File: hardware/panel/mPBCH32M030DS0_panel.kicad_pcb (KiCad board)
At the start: 2 copper layers, 97.9 x 95.6 mm, 315 parts, among them J1 EDGE_L, J1 SOCK_L, J2 EDGE_R, J2 SOCK_R, J3 PWR_IN, J4 MOTOR, J8 USB-C, Q1 MTN2306AN3, Q1 TKR74F04PB, Q1 TPN1R603PL, Q10 TPN1R603PL, Q2 MTN2306AN3, Q2 TKR74F04PB, Q2 TPN1R603PL, Q3 MTN2306AN3, Q3 TKR74F04PB, Q3 TPN1R603PL, Q4 MTN2306AN3, Q4 TKR74F04PB, Q4 TPN1R603PL, Q5 MTN2306AN3, Q5 TKR74F04PB, Q5 TPN1R603PL, Q6 MTN2306AN3, Q6 TKR74F04PB, Q6 TPN1R603PL, Q7 MTN2306AN3, Q7 TKR74F04PB, Q7 TPN1R603PL, Q8 MTN2306AN3, Q8 TKR74F04PB, Q8 TPN1R603PL, Q9 TPN2R304PL, SW1 RESET, SW2 USER/BOOT, U1 CH32M030C8U7, U2 78L05, U3 USBLC6-2SC6, U4 LM74700-Q1, U5 LM74700-Q1, Y1 8MHz CL=20pF

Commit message: 面付けパネルを A/C 74.9mm に合わせて更新, 製造データと資料を最新の A/C に
- gen_panel.py: A/C の長さ 70.74 → 74.9mm (パネル 97.9 × 99.8mm)。タブを銅の無い区間へ移動
  (A の右辺は J2 沿いの GND 配線があるため A↔C / C↔B のタブは下寄り)
- 各基板の製造データ (hardware/fab/*.zip) と DRC 集計を再生成
- README / stacking.md: A/C の寸法・電流の目安 (A 約 5A/相 はんだ盛り時, C 約 3A/相) とレイアウトの説明,
  電源ベタのはんだ盛りの注意 (低温はんだ不可, 下面は盛り 0.3〜0.5mm 以下), J3/J4 の向き, D9 を外した理由
- B はレイアウト見直し中と明記 (現状の配線は約 1A まで)

Co-Authored-By: Claude Opus 5.5 <noreply@anthropic.com>
Claude-Session: https://claude.ai/code/session_01LENFjjhDfYjJZV1NWhB9uV
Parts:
- removed the C1 at (39.9, 45.7)
- removed the C1 at (15.1, 55.3)
- removed the C3 at (15.4, 10.4)
- removed the C3 at (40.3, 10.4)
- removed the C30 at (17.8, 46.1)
- removed the C30 at (42.7, 45.7)
- removed the C31 at (18.6, 42.5)
- removed the C31 at (40.4, 42.1)
- removed the C4 at (18.1, 10.1)
- removed the C4 at (43.0, 10.1)
- removed the C40 at (17.8, 34.4)
- removed the C40 at (42.7, 34.1)
- removed the C41 at (40.4, 30.5)
- removed the C41 at (18.6, 30.8)
- removed the C5 at (18.8, 41.0)
- removed the C5 at (43.7, 31.4)
- removed the C50 at (42.7, 22.5)
- removed the C50 at (17.8, 22.7)
- removed the C51 at (40.4, 18.9)
- removed the C51 at (18.6, 19.1)
- removed the C6 at (17.7, 5.79)
- removed the C6 at (42.6, 5.79)
- removed the C60 at (42.7, 10.8)
- removed the C60 at (17.8, 11.0)
- removed the C61 at (18.6, 7.39)
- removed the C61 at (40.4, 7.24)
- removed the C7 at (14.8, 24.0)
- removed the C7 at (39.7, 24.0)
- removed the C71 at (37.2, 22.5)
- removed the C71 at (15.2, 53.8)
- removed the C72 at (38.4, 34.1)
- removed the C72 at (18.7, 53.8)
- removed the C73 at (37.2, 45.7)
- removed the C73 at (22.2, 53.8)
- removed the C8 at (14.8, 33.6)
- removed the D1 at (11.7, 48.6)
- removed the D1 at (36.6, 39.0)
- removed the D9 at (37.9, 7.08)
- removed the D9 at (13.0, 7.08)
- removed the F1 at (38.4, 32.7)
- removed the F1 at (13.5, 42.3)
- removed the F3 at (37.3, 2.60)
- removed the F3 at (12.4, 2.60)
- removed the J3 at (34.9, 62.1)
- removed the J3 at (10.1, 62.1)
- removed the J4 at (32.4, 68.7)
- removed the J4 at (7.55, 68.7)
- removed the JP5 at (40.5, 50.1)
- removed the JP5 at (18.7, 50.3)
- removed the JP7 at (35.6, 55.0)
- removed the JP7 at (10.7, 55.2)
- removed the MB at (0.00, 0.00) (x9)
- removed the Q1 at (11.7, 38.1)
- removed the Q1 at (36.3, 37.8)
- removed the Q10 at (17.9, 2.42)
- removed the Q10 at (42.8, 2.42)
- removed the Q2 at (16.5, 38.1)
- removed the Q2 at (40.6, 37.8)
- removed the Q3 at (11.7, 26.4)
- removed the Q3 at (36.3, 26.2)
- removed the Q4 at (16.5, 26.4)
- removed the Q4 at (40.6, 26.2)
- removed the Q5 at (11.7, 14.7)
- removed the Q5 at (36.3, 14.6)
- removed the Q6 at (40.6, 14.6)
- removed the Q6 at (16.5, 14.7)
- removed the Q7 at (36.3, 2.94)
- removed the Q7 at (11.7, 3.02)
- removed the Q8 at (40.6, 2.94)
- removed the Q8 at (16.5, 3.02)
- removed the Q9 at (41.4, 37.1)
- removed the Q9 at (16.5, 46.7)
- removed the R11 at (10.4, 39.3)
- removed the R11 at (35.3, 29.7)
- removed the R12 at (12.6, 39.3)
- removed the R12 at (37.5, 29.7)
- removed the R30 at (22.9, 46.1)
- removed the R30 at (47.8, 45.7)
- removed the R31 at (19.1, 46.1)
- removed the R31 at (43.9, 45.7)
- removed the R32 at (46.5, 45.7)
- removed the R32 at (21.6, 46.1)
- removed the R33 at (20.4, 46.1)
- removed the R33 at (45.2, 45.7)
- removed the R34 at (36.6, 40.9)
- removed the R34 at (13.3, 42.1)
- removed the R40 at (22.9, 34.4)
- removed the R40 at (47.8, 34.1)
- removed the R41 at (43.9, 34.1)
- removed the R41 at (19.1, 34.4)
- removed the R42 at (21.6, 34.4)
- removed the R42 at (46.5, 34.1)
- removed the R43 at (45.2, 34.1)
- removed the R43 at (20.4, 34.4)
- removed the R44 at (36.6, 29.3)
- removed the R44 at (13.3, 30.4)
- removed the R50 at (22.9, 22.7)
- removed the R50 at (47.8, 22.5)
- removed the R51 at (43.9, 22.5)
- removed the R51 at (19.1, 22.7)
- removed the R52 at (46.5, 22.5)
- removed the R52 at (21.6, 22.7)
- removed the R53 at (45.2, 22.5)
- removed the R53 at (20.4, 22.7)
- removed the R54 at (13.3, 18.7)
- removed the R54 at (36.6, 17.7)
- removed the R6 at (19.9, 5.80)
- removed the R6 at (44.8, 5.80)
- removed the R60 at (22.9, 11.0)
- removed the R60 at (47.8, 10.9)
- removed the R61 at (19.1, 11.0)
- removed the R61 at (43.9, 10.9)
- removed the R62 at (46.5, 10.9)
- removed the R62 at (21.6, 11.0)
- removed the R63 at (45.2, 10.9)
- removed the R63 at (20.4, 11.0)
- removed the R64 at (13.3, 7.01)
- removed the R64 at (36.6, 6.05)
- removed the R70 at (36.6, 48.9)
- removed the R70 at (13.3, 49.9)
- removed the R71 at (12.8, 53.8)
- removed the R71 at (34.8, 22.5)
- removed the R72 at (14.0, 53.8)
- removed the R72 at (36.0, 22.5)
- removed the R74 at (36.0, 34.1)
- removed the R74 at (16.3, 53.8)
- removed the R75 at (17.5, 53.8)
- removed the R75 at (37.2, 34.1)
- removed the R77 at (34.8, 45.7)
- removed the R77 at (19.8, 53.8)
- removed the R78 at (36.0, 45.7)
- removed the R78 at (21.0, 53.8)
- removed the TH1 at (34.8, 34.1)
- removed the TH1 at (9.96, 34.4)
- removed the U2 at (37.2, 16.3)
- removed the U2 at (12.3, 16.3)
- removed the U4 at (11.5, 54.7)
- removed the U4 at (36.4, 45.1)
- removed the U5 at (36.4, 11.3)
- removed the U5 at (11.5, 11.3)
- added C1: 10uF/50V, C_1206_3216Metric, B.Cu at (38.5, 70.4)
- added C1: 10uF/50V, C_1206_3216Metric, B.Cu at (13.6, 70.4)
- added C120: 1nF/50V, C_0402_1005Metric, B.Cu at (31.4, 87.0)
- added C3: 1uF/50V, C_0603_1608Metric, B.Cu at (22.1, 2.12)
- added C3: 1uF/50V, C_0603_1608Metric, B.Cu at (46.9, 2.12)
- added C30: 0.1uF/50V, C_0402_1005Metric, B.Cu at (11.4, 42.4)
- added C30: 0.1uF/50V, C_0402_1005Metric, B.Cu at (36.5, 42.4)
- added C31: 10uF/25V, C_0805_2012Metric, B.Cu at (12.9, 42.4)
- added C31: 10uF/25V, C_0805_2012Metric, B.Cu at (38.2, 42.0)
- added C4: 1uF/25V, C_0402_1005Metric, B.Cu at (21.8, 4.75)
- added C4: 1uF/25V, C_0402_1005Metric, B.Cu at (46.7, 4.75)
- added C40: 0.1uF/50V, C_0402_1005Metric, B.Cu at (36.5, 33.4)
- added C40: 0.1uF/50V, C_0402_1005Metric, B.Cu at (11.4, 33.4)
- added C41: 10uF/25V, C_0805_2012Metric, B.Cu at (38.2, 33.0)
- added C41: 10uF/25V, C_0805_2012Metric, B.Cu at (12.9, 33.4)
- added C5: 0.1uF/50V, C_0402_1005Metric, B.Cu at (12.9, 60.8)
- added C5: 0.1uF/50V, C_0402_1005Metric, B.Cu at (37.8, 60.8)
- added C50: 0.1uF/50V, C_0402_1005Metric, B.Cu at (11.4, 24.4)
- added C50: 0.1uF/50V, C_0402_1005Metric, B.Cu at (36.5, 24.4)
- added C51: 10uF/25V, C_0805_2012Metric, B.Cu at (38.2, 24.0)
- added C51: 10uF/25V, C_0805_2012Metric, B.Cu at (12.9, 24.4)
- added C6: 0.1uF/50V, C_0402_1005Metric, B.Cu at (13.2, 8.95)
- added C6: 0.1uF/50V, C_0402_1005Metric, B.Cu at (38.1, 8.95)
- added C60: 0.1uF/50V, C_0402_1005Metric, B.Cu at (36.5, 15.4)
- added C60: 0.1uF/50V, C_0402_1005Metric, B.Cu at (11.4, 15.4)
- added C61: 10uF/25V, C_0805_2012Metric, B.Cu at (12.9, 15.4)
- added C61: 10uF/25V, C_0805_2012Metric, B.Cu at (38.2, 15.0)
- added C7: 100uF/25V, CP_Elec_8x6.2, F.Cu at (39.8, 4.72)
- added C7: 150uF/25V, CP_Elec_8x6.2, F.Cu at (14.9, 4.72)
- added C71: 1nF/50V, C_0402_1005Metric, B.Cu at (12.9, 48.1)
- added C71: 1nF/50V, C_0402_1005Metric, B.Cu at (37.8, 48.1)
- added C72: 1nF/50V, C_0402_1005Metric, B.Cu at (37.8, 50.2)
- added C72: 1nF/50V, C_0402_1005Metric, B.Cu at (12.9, 50.2)
- added C73: 1nF/50V, C_0402_1005Metric, B.Cu at (12.9, 52.4)
- added C73: 1nF/50V, C_0402_1005Metric, B.Cu at (37.8, 52.4)
- added D1: SMBJ16A, D_SMB, B.Cu at (38.5, 65.2)
- added D1: SMBJ16A, D_SMB, B.Cu at (13.6, 65.2)
- added F1: 5A, Fuse_Littelfuse_NANO2_2410, F.Cu at (39.1, 63.1)
- added F1: 7A, Fuse_Littelfuse_NANO2_2410, F.Cu at (14.2, 63.1)
- added F3: 5A, Fuse_1812_4532Metric, B.Cu at (13.4, 2.60)
- added F3: 5A, Fuse_1812_4532Metric, B.Cu at (38.3, 2.60)
- added J3: PWR_IN, PinHeader_2x06_P2.54mm_Vertical, F.Cu at (10.1, 68.4)
- added J3: PWR_IN, PinHeader_2x06_P2.54mm_Vertical, F.Cu at (34.9, 68.4)
- added J4: MOTOR, PinHeader_2x08_P2.54mm_Vertical, F.Cu at (50.2, 73.5)
- added J4: MOTOR, PinHeader_2x08_P2.54mm_Vertical, F.Cu at (25.3, 73.5)
- added JP5: ISEL_B, SolderJumper-3_P1.3mm_Bridged12_RoundedPad1.0x1.5mm_NumberLabels, F.Cu at (11.0, 27.0)
- added JP5: ISEL_B, SolderJumper-3_P1.3mm_Bridged12_RoundedPad1.0x1.5mm_NumberLabels, F.Cu at (35.9, 27.0)
- added JP7: ISEL_A, SolderJumper-3_P1.3mm_Bridged12_RoundedPad1.0x1.5mm_NumberLabels, F.Cu at (11.0, 42.6)
- added JP7: ISEL_A, SolderJumper-3_P1.3mm_Bridged12_RoundedPad1.0x1.5mm_NumberLabels, F.Cu at (35.9, 42.6)
- added MB (x9): , , F.Cu at (0.00, 0.00)
- added Q1: TPN1R603PL, Vishay_PowerPAK_1212-8_Single, B.Cu at (16.3, 44.0)
- added Q1: MTN2306AN3, SOT-23, B.Cu at (41.2, 40.2)
- added Q10: TPN1R603PL, Vishay_PowerPAK_1212-8_Single, B.Cu at (43.7, 2.42)
- added Q10: TPN1R603PL, Vishay_PowerPAK_1212-8_Single, B.Cu at (18.9, 2.42)
- added Q2: MTN2306AN3, SOT-23, B.Cu at (41.2, 43.9)
- added Q2: TPN1R603PL, Vishay_PowerPAK_1212-8_Single, B.Cu at (16.3, 40.2)
- added Q3: TPN1R603PL, Vishay_PowerPAK_1212-8_Single, B.Cu at (16.3, 35.0)
- added Q3: MTN2306AN3, SOT-23, B.Cu at (41.2, 31.2)
- added Q4: MTN2306AN3, SOT-23, B.Cu at (41.2, 34.9)
- added Q4: TPN1R603PL, Vishay_PowerPAK_1212-8_Single, B.Cu at (16.3, 31.2)
- added Q5: TPN1R603PL, Vishay_PowerPAK_1212-8_Single, B.Cu at (16.3, 26.0)
- added Q5: MTN2306AN3, SOT-23, B.Cu at (41.2, 22.2)
- added Q6: MTN2306AN3, SOT-23, B.Cu at (41.2, 25.9)
- added Q6: TPN1R603PL, Vishay_PowerPAK_1212-8_Single, B.Cu at (16.3, 22.2)
- added Q7: TPN1R603PL, Vishay_PowerPAK_1212-8_Single, B.Cu at (16.3, 17.0)
- added Q7: MTN2306AN3, SOT-23, B.Cu at (41.2, 13.2)
- added Q8: MTN2306AN3, SOT-23, B.Cu at (41.2, 16.9)
- added Q8: TPN1R603PL, Vishay_PowerPAK_1212-8_Single, B.Cu at (16.3, 13.2)
- added Q9: TPN2R304PL, Vishay_PowerPAK_1212-8_Single, F.Cu at (14.2, 56.6)
- added Q9: TPN2R304PL, Vishay_PowerPAK_1212-8_Single, F.Cu at (39.1, 56.6)
- added R11: 110k 1%, R_0402_1005Metric, B.Cu at (38.9, 47.9)
- added R11: 110k 1%, R_0402_1005Metric, B.Cu at (14.3, 46.5)
- added R12: 10k 1%, R_0402_1005Metric, B.Cu at (40.2, 47.9)
- added R12: 10k 1%, R_0402_1005Metric, B.Cu at (16.3, 46.5)
- added R30: 47R, R_0402_1005Metric, B.Cu at (44.4, 39.3)
- added R30: 47R, R_0805_2012Metric, B.Cu at (20.6, 36.8)
- added R31: 20k, R_0402_1005Metric, B.Cu at (19.1, 44.0)
- added R31: 20k, R_0402_1005Metric, B.Cu at (45.5, 40.1)
- added R32: 47R, R_0402_1005Metric, B.Cu at (44.4, 44.8)
- added R32: 47R, R_0805_2012Metric, B.Cu at (22.7, 36.8)
- added R33: 20k, R_0402_1005Metric, B.Cu at (13.1, 37.4)
- added R33: 20k, R_0402_1005Metric, B.Cu at (41.1, 46.4)
- added R34: 10mR 1% 0.5W, R_1206_3216Metric, B.Cu at (11.7, 39.4)
- added R34: 10mR 1% 0.5W, R_1206_3216Metric, B.Cu at (36.6, 45.2)
- added R40: 47R, R_0805_2012Metric, B.Cu at (20.6, 29.2)
- added R40: 47R, R_0402_1005Metric, B.Cu at (44.4, 30.3)
- added R41: 20k, R_0402_1005Metric, B.Cu at (19.1, 35.0)
- added R41: 20k, R_0402_1005Metric, B.Cu at (45.5, 31.1)
- added R42: 47R, R_0805_2012Metric, B.Cu at (22.7, 29.2)
- added R42: 47R, R_0402_1005Metric, B.Cu at (44.4, 35.8)
- added R43: 20k, R_0402_1005Metric, B.Cu at (13.1, 28.4)
- added R43: 20k, R_0402_1005Metric, B.Cu at (41.1, 37.4)
- added R44: 10mR 1% 0.5W, R_1206_3216Metric, B.Cu at (36.6, 36.2)
- added R44: 10mR 1% 0.5W, R_1206_3216Metric, B.Cu at (11.7, 30.4)
- added R50: 47R, R_0402_1005Metric, B.Cu at (44.4, 21.3)
- added R50: 47R, R_0805_2012Metric, B.Cu at (20.6, 21.6)
- added R51: 20k, R_0402_1005Metric, B.Cu at (45.5, 22.1)
- added R51: 20k, R_0402_1005Metric, B.Cu at (19.1, 26.0)
- added R52: 47R, R_0402_1005Metric, B.Cu at (44.4, 26.8)
- added R52: 47R, R_0805_2012Metric, B.Cu at (22.7, 21.6)
- added R53: 20k, R_0402_1005Metric, B.Cu at (41.1, 28.4)
- added R53: 20k, R_0402_1005Metric, B.Cu at (13.1, 19.4)
- added R54: 10mR 1% 0.5W, R_1206_3216Metric, B.Cu at (11.7, 21.4)
- added R54: 10mR 1% 0.5W, R_1206_3216Metric, B.Cu at (36.6, 27.2)
- added R6: 100k, R_0402_1005Metric, B.Cu at (10.2, 5.70)
- added R6: 100k, R_0402_1005Metric, B.Cu at (35.1, 5.70)
- added R60: 47R, R_0402_1005Metric, B.Cu at (44.4, 12.3)
- added R60: 47R, R_0805_2012Metric, B.Cu at (20.6, 14.0)
- added R61: 20k, R_0402_1005Metric, B.Cu at (45.5, 13.1)
- added R61: 20k, R_0402_1005Metric, B.Cu at (19.1, 17.0)
- added R62: 47R, R_0402_1005Metric, B.Cu at (44.4, 17.8)
- added R62: 47R, R_0805_2012Metric, B.Cu at (22.7, 14.0)
- added R63: 20k, R_0402_1005Metric, B.Cu at (41.1, 19.4)
- added R63: 20k, R_0402_1005Metric, B.Cu at (13.1, 10.4)
- added R64: 10mR 1% 0.5W, R_1206_3216Metric, B.Cu at (11.7, 12.4)
- added R64: 10mR 1% 0.5W, R_1206_3216Metric, B.Cu at (36.6, 18.2)
- added R70: 10mR 1% 0.5W, R_1206_3216Metric, B.Cu at (9.75, 49.0)
- added R70: 10mR 1% 0.5W, R_1206_3216Metric, B.Cu at (34.6, 49.0)
- added R71: 20k 1%, R_0402_1005Metric, B.Cu at (17.2, 47.6)
- added R71: 20k 1%, R_0402_1005Metric, B.Cu at (42.1, 49.4)
- added R72: 3k 1%, R_0402_1005Metric, B.Cu at (11.8, 48.1)
- added R72: 3k 1%, R_0402_1005Metric, B.Cu at (36.7, 48.1)
- added R74: 20k 1%, R_0402_1005Metric, B.Cu at (44.1, 50.5)
- added R74: 20k 1%, R_0402_1005Metric, B.Cu at (19.2, 48.7)
- added R75: 3k 1%, R_0402_1005Metric, B.Cu at (11.8, 50.2)
- added R75: 3k 1%, R_0402_1005Metric, B.Cu at (36.7, 50.2)
- added R77: 20k 1%, R_0402_1005Metric, B.Cu at (46.2, 51.6)
- added R77: 20k 1%, R_0402_1005Metric, B.Cu at (21.3, 49.8)
- added R78: 3k 1%, R_0402_1005Metric, B.Cu at (11.8, 52.4)
- added R78: 3k 1%, R_0402_1005Metric, B.Cu at (36.7, 52.4)
- added TH1: 10k B3435, R_0402_1005Metric, F.Cu at (11.1, 46.6)
- added TH1: 10k B3435, R_0402_1005Metric, F.Cu at (36.0, 46.6)
- added U2: 78L05, SOT-89-3, B.Cu at (43.8, 7.20)
- added U2: 78L05, SOT-89-3, B.Cu at (18.9, 7.20)
- added U4: LM74700-Q1, SOT-23-6, B.Cu at (38.3, 58.2)
- added U4: LM74700-Q1, SOT-23-6, B.Cu at (13.4, 58.2)
- added U5: LM74700-Q1, SOT-23-6, B.Cu at (13.2, 6.50)
- added U5: LM74700-Q1, SOT-23-6, B.Cu at (38.1, 6.50)
- moved J3 4.16 mm to (70.0, 66.3)
- moved C1 4.16 mm to (75.3, 45.8)
- moved C3 4.16 mm to (63.3, 25.4)
- moved C30 4.16 mm to (92.8, 42.2)
- moved C31 4.16 mm to (64.3, 49.9)
- moved C40 4.16 mm to (92.8, 34.6)
- moved C41 4.16 mm to (64.3, 44.8)
- moved C5 4.16 mm to (79.1, 31.8)
- moved C50 4.16 mm to (92.8, 27.0)
- moved C51 4.16 mm to (64.3, 39.7)
- moved C6 4.16 mm to (56.7, 18.6)
- moved C61 4.16 mm to (64.3, 34.6)
- moved C71 4.16 mm to (71.5, 53.5)
- moved C72 4.16 mm to (75.2, 53.5)
- moved C73 4.16 mm to (78.9, 53.5)
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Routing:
- net A/VBUS: track 152.7 -> 40.9 mm, vias 10 -> 30
- net C/SW0: track 117.5 -> 9.31 mm, vias 0 -> 9
- net C/SW2: track 107.4 -> 6.55 mm, vias 2 -> 5
- net A/SW3: track 114.2 -> 13.9 mm, vias 2 -> 8
- net A/SW2: track 109.6 -> 14.7 mm, vias 1 -> 9
- net C/SW3: track 87.1 -> 4.93 mm, vias 2 -> 4
- net C/ISH: track 77.9 -> 1.55 mm
- net C/SW1: track 82.0 -> 7.93 mm, vias 2 -> 5
- net A/SW1: track 89.6 -> 16.4 mm, vias 1 -> 9
- net C/VBUS: track 110.9 -> 41.0 mm, vias 5 -> 33
- net A/ISH: track 64.8 -> 1.55 mm
- net C/SRC2: track 61.3 -> 4.48 mm, vias 3 -> 1
- net A/SW0: track 71.8 -> 19.2 mm, vias 2 -> 13
- net A/SRC2: track 55.2 -> 2.97 mm, vias 3 -> 1
- net A/GND: track 193.5 -> 143.0 mm, vias 4 -> 6
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- added copper zone on B.Cu, net A/USB_VBUS_P
- added copper zone on B.Cu, net A/VIN_F
- added copper zone on B.Cu, net C/USB_VBUS_P
- added copper zone on B.Cu, net C/VIN_F
- removed copper zone on F.Cu, net A/SRC1
- removed copper zone on F.Cu, net A/SRC2
- removed copper zone on F.Cu, net A/USB_VBUS_P
- removed copper zone on B.Cu, net A/VIN
- removed copper zone on F.Cu, net C/SRC1
- removed copper zone on F.Cu, net C/SRC2
- removed copper zone on F.Cu, net C/USB_VBUS_P
- removed copper zone on B.Cu, net C/VIN
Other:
- board size 97.9 x 95.6 mm -> 97.9 x 99.8 mm
- board text added: "OUT3..0"
- board text added: "VIN/GND"

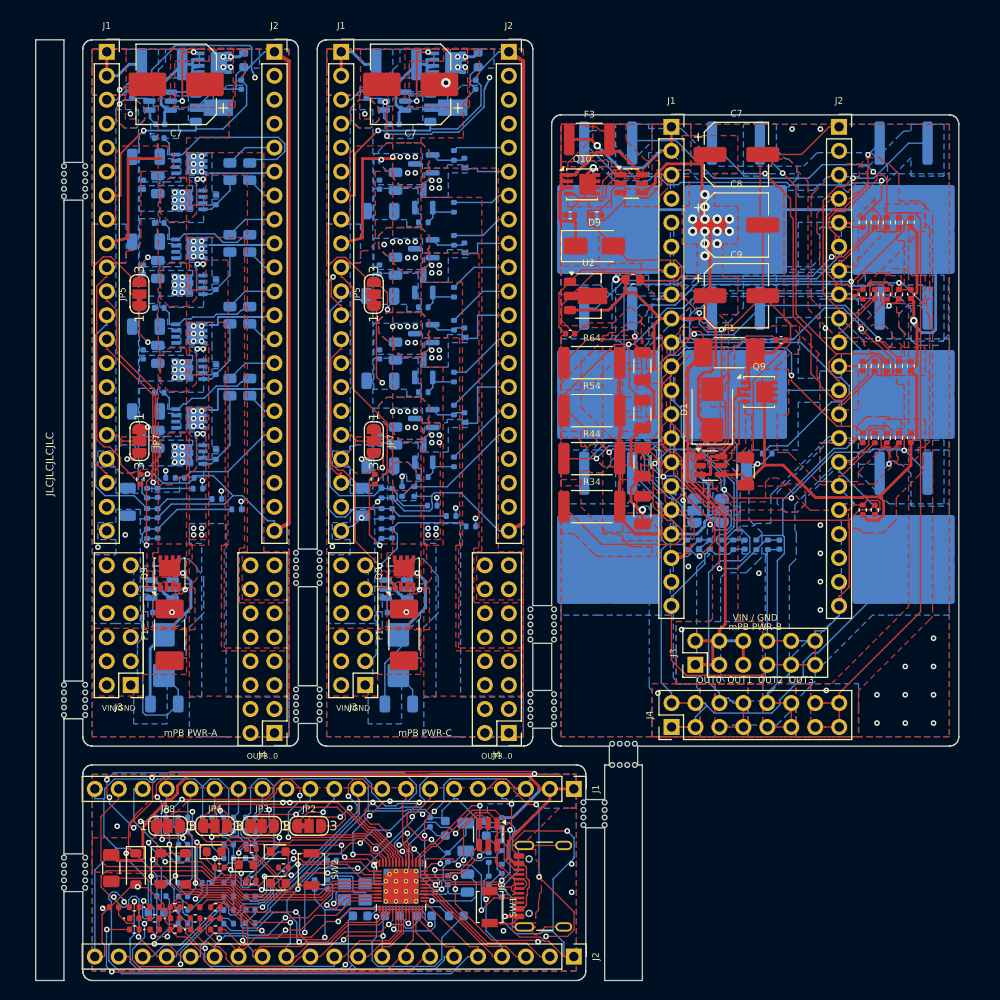
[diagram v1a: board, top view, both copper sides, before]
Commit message: 子基板 B を 44.6 x 99.5mm に拡大: M3 丸端子台 x6・ヒートシンク固定穴 x2・電源ベタのはんだ盛り
- 電源 (J3 VIN / J5 GND) と 4 相出力 (J40〜J43) を Würth REDCUBE の M3 丸端子台で受ける
- ヒートシンク固定用 M3 穴 H1/H2。MOSFET・シャントは BOTTOM 面 (ヒートシンク側) に 4 レッグ横並び
- 大電流の銅箔を配線前に固定ベタとして置き, レジスト開口ではんだを盛れるようにした
- 右端の VBUS 帯を表裏 2 層に, レッグ 3 横のネックを裏で迂回, 上端に USB 帰路の GND 帯
- 電流容量 (1 相): 1oz 5.4A / はんだ 0.3mm 7.4A。USB-PD 経路は 3A まで
- D1/C1 の − 側は ISH。面付けパネル (99.94 x 99.76mm), 製造データ, 資料を更新

Co-Authored-By: Claude Opus 5.5 <noreply@anthropic.com>
Claude-Session: https://claude.ai/code/session_01LENFjjhDfYjJZV1NWhB9uV
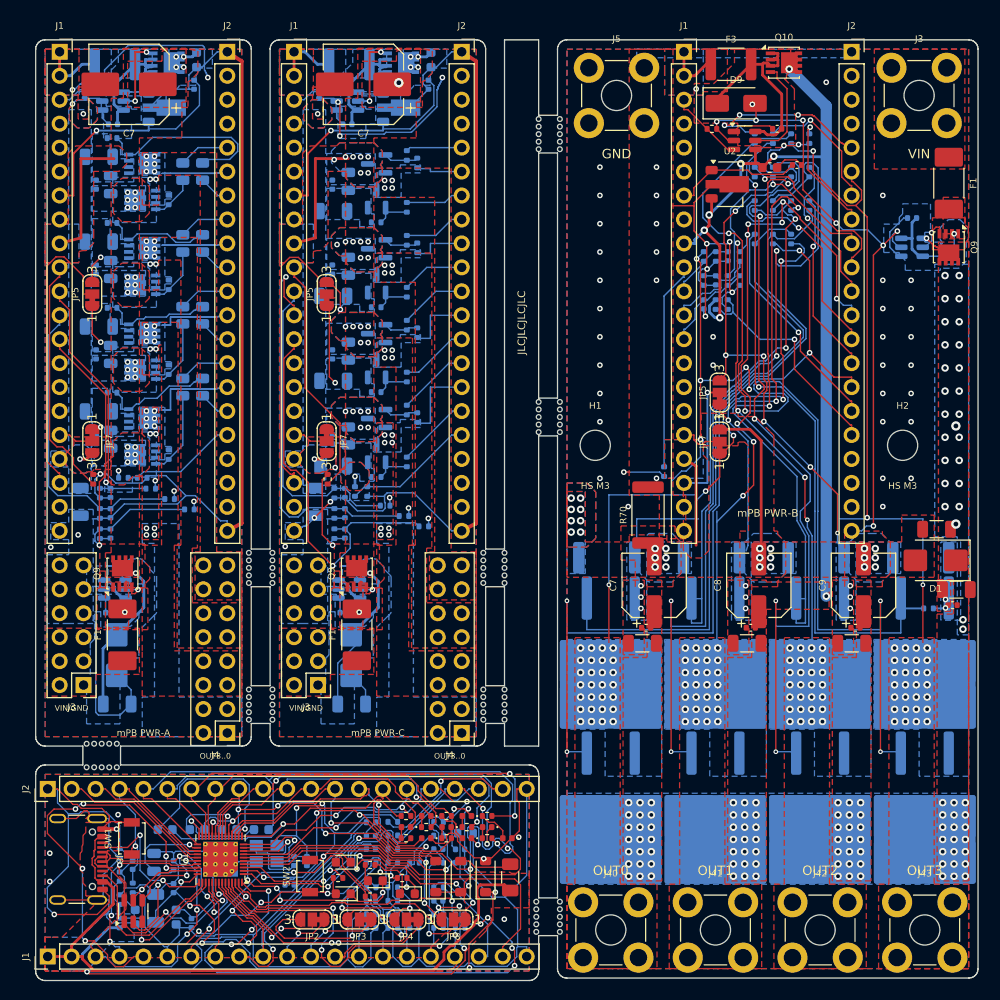
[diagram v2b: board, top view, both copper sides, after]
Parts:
- removed the J4 at (67.4, 72.9)
- removed the MB at (0.00, 0.00) (x9)
- added H1: HEATSINK_M3, MountingHole_3.2mm_M3, F.Cu at (59.3, 43.0)
- added H2: HEATSINK_M3, MountingHole_3.2mm_M3, F.Cu at (91.9, 43.0)
- added J40: OUT0, Wuerth_REDCUBE-THR_WP-THRBU_74650073_THR, F.Cu at (61.0, 94.4)
- added J41: OUT1, Wuerth_REDCUBE-THR_WP-THRBU_74650073_THR, F.Cu at (72.1, 94.4)
- added J42: OUT2, Wuerth_REDCUBE-THR_WP-THRBU_74650073_THR, F.Cu at (83.2, 94.4)
- added J43: OUT3, Wuerth_REDCUBE-THR_WP-THRBU_74650073_THR, F.Cu at (94.3, 94.4)
- added J5: GND, Wuerth_REDCUBE-THR_WP-THRBU_74650073_THR, F.Cu at (61.6, 5.90)
- added MB (x8): , , F.Cu at (0.00, 0.00)
- C5, R11, R12, R30, R31, R32, R33, R34, R40, R41, R42, R43, R44, R50, R51, R52, R53, R54, R60, R61, R62, R63, R64, U4: moved to B.Cu
- J3: value PWR_IN -> VIN; footprint PinHeader_2x06_P2.54mm_Vertical -> Wuerth_REDCUBE-THR_WP-THRBU_74650073_THR
- JP5, JP7, R70: moved to F.Cu
- moved Q7 72.9 mm to (94.3, 83.3)
- moved Q5 65.3 mm to (83.2, 83.3)
- moved J3 64.9 mm to (93.7, 5.90), turned to 0 degrees
- moved Q3 64.7 mm to (72.1, 83.3)
- moved J1 58.6 mm to (1.27, 97.2), turned to 90 degrees
- moved J2 58.6 mm to (1.27, 79.4), turned to 90 degrees
- moved J8 51.6 mm to (3.41, 86.9), turned to -90 degrees
- moved C7 46.5 mm to (65.6, 57.9), turned to 90 degrees
- moved Q8 45.5 mm to (94.3, 66.8)
- moved D17 42.3 mm to (50.0, 84.7), turned to 180 degrees
- moved F2 42.3 mm to (50.3, 88.8), turned to 90 degrees
- moved R7 41.9 mm to (8.91, 93.7), turned to 90 degrees
- moved R63 41.1 mm to (94.7, 60.3), turned to 0 degrees
- moved R8 40.9 mm to (8.91, 91.2), turned to 90 degrees
- moved C61 40.9 mm to (97.6, 58.3), turned to 180 degrees
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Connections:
- C1 pad 2: B/GND -> B/ISH
- C7 pad 2: B/GND -> B/ISH
- C8 pad 2: B/GND -> B/ISH
- C9 pad 2: B/GND -> B/ISH
- D1 pad 2: B/GND -> B/ISH
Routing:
- net B/VBUS: track 253.3 -> 97.6 mm, vias 17 -> 118
- net B/GND: track 213.3 -> 115.4 mm, vias 20 -> 51
- net B/SW3: track 160.3 -> 71.0 mm, vias 2 -> 31
- net B/GH3: track 41.2 -> 106.9 mm, vias 1 -> 4
- net B/GH2: track 26.5 -> 91.3 mm, vias 1 -> 6
- net B/GL2: track 5.04 -> 67.9 mm, vias 1 -> 2
- net B/GL0: track 6.77 -> 69.1 mm, vias 1 -> 0
- net B/GH1: track 44.0 -> 91.8 mm, vias 1 -> 4
- net B/SRC3: track 48.3 -> 1.04 mm
- net B/VIN: track 45.9 -> 0.00 mm, vias 1 -> 0
- net B/GH0: track 51.0 -> 92.8 mm, vias 1 -> 2
- net B/GL3: track 39.0 -> 73.1 mm, vias 1 -> 2
- net B/SW2: track 102.7 -> 71.8 mm, vias 2 -> 33
- net B/SW1: track 104.9 -> 74.7 mm, vias 1 -> 36
- net B/SRC2: track 75.7 -> 53.9 mm, vias 3 -> 9
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- added copper zone on B.Cu, net B/VIN_F
- removed copper zone on B.Cu, net B/VIN
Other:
- board size 97.9 x 99.8 mm -> 99.9 x 99.8 mm
- board text added: "HS M3"
- board text added: "OUT0"
- board text added: "OUT1"
- board text added: "OUT2"
- board text added: "OUT3"
- board text added: "VIN"
- board text removed: "OUT0 OUT1 OUT2 OUT3"
- board text removed: "VIN / GND"

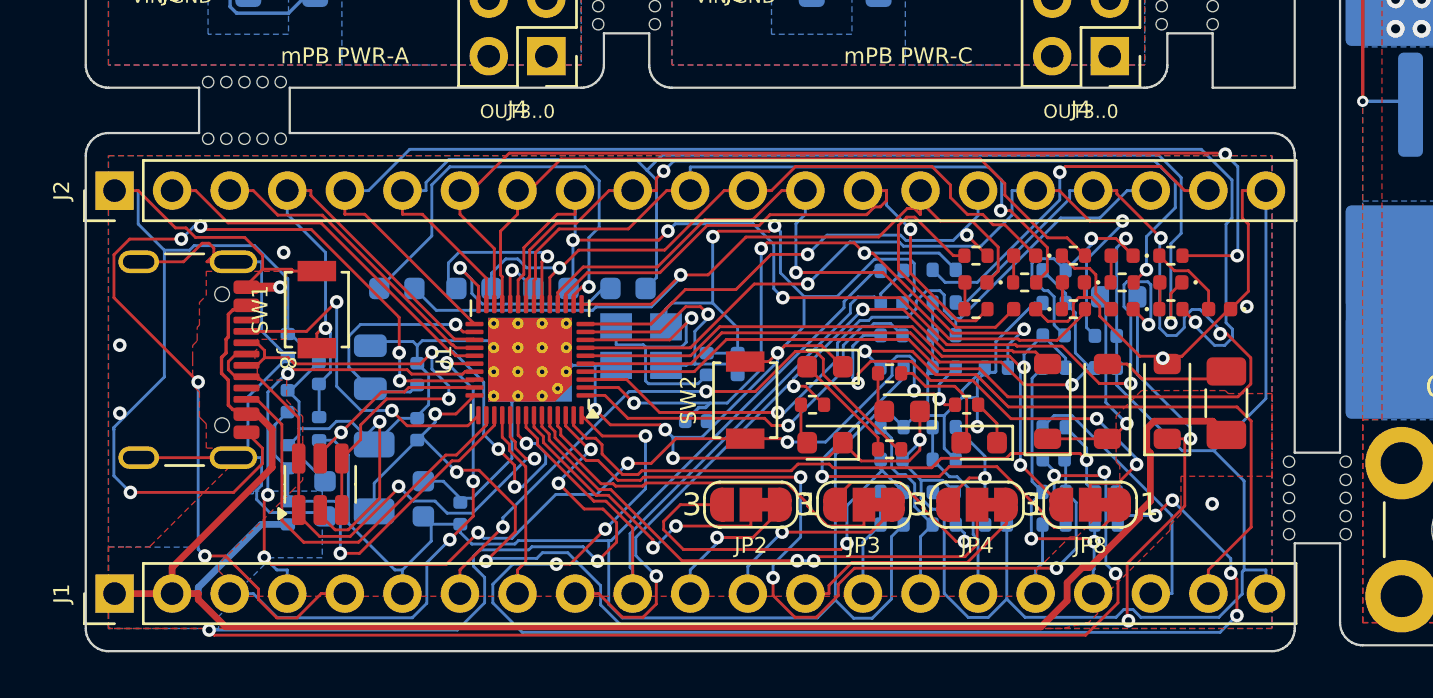
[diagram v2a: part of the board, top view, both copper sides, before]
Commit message: MCU モジュール: ピンヘッダを下面実装に (ピンは MCU と反対側), ピン番号を上面シルクに
- J1/J2 を BOTTOM 面へ裏返した (180° 回転 + 反転で 1 番ピンは上端のまま, 穴の位置は不変)。
  ブレッドボード・子基板のソケットに挿しても USB-C とボタンが上を向き, 操作できる
- 上面 (MCU 側) の各ピンの外側にピン番号 1〜21, 下面の信号名は樹脂部の外 (1.5mm) へ
- 配線は確定済みのものをそのまま使う (tools/module_headers_bottom.py)。gen_pcb.py main で作り直す場合も
  配線後に裏返す (flip_after_route)
- DRC: 電気的エラー 0 / 未接続 0。3D: 単体・子基板 A/B に挿した状態とも干渉なし
- 手直し用ベタなし版, 製造データ, パネル, 資料を更新

Co-Authored-By: Claude Opus 5.5 <noreply@anthropic.com>
Claude-Session: https://claude.ai/code/session_01LENFjjhDfYjJZV1NWhB9uV
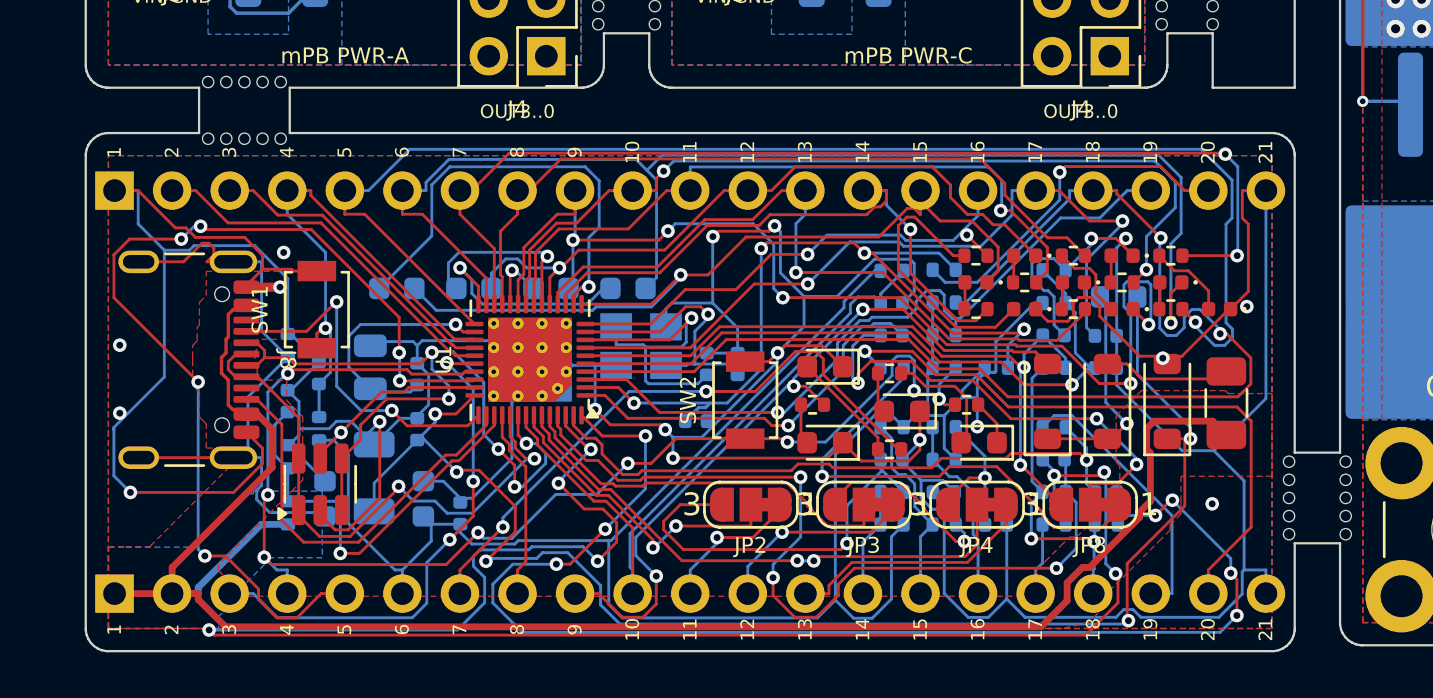
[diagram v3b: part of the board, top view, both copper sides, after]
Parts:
- removed the MB at (0.00, 0.00) (x8)
- added MB (x8): , , F.Cu at (0.00, 0.00)
- J1, J2: moved to B.Cu
- turned J1 to -90 degrees
- turned J2 to -90 degrees
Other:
- board text added: "1"
- board text added: "10"
- board text added: "11"
- board text added: "12"
- board text added: "13"
- board text added: "14"
- board text added: "15"
- board text added: "16"
- board text added: "17"
- board text added: "18"
- board text added: "19"
- board text added: "2"
- board text added: "20"
- board text added: "21"
- board text added: "3"
- board text added: "4"
- board text added: "5"
- board text added: "6"
- board text added: "7"
- board text added: "8"
- board text added: "9"
